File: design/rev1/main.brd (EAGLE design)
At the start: 78 x 50 mm, 43 parts, among them J1 ICSP-HEADER1X6-0.1-ICSP-PADS, J2 HEADER-141X14-0.1-PADS, SW1 JS102000SAQN, SW2 JS102000SAQN, SW3 B3U-3000P, U1 PIC18F2XK20, U2 LIS3DSH, U3 APDS-9008

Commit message: [CNG] - more schematic and layout progress on rev1
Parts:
- added C7: 0.1uF, matt:SMD-0603
- C2: device matt:SMD-0805 -> matt:SMD-0603
- D1, D10, D2, D3, D4, D5, D6, D7, D8, D9: value LED0402 -> LED0603; device matt:SMD-0402-P -> matt:SMD-0603-P
- J2: value HEADER-141X14-0.1-PADS -> HEADER-141X14-0.05-PADS; device matt:1X14-0.1-PADS -> matt:1X14-0.05-PADS
- moved SW3 59.3 mm to (13.0, 48.0), turned to 0 degrees
- moved L1 30.1 mm to (53.7, 26.0)
- moved REG1 30.1 mm to (49.8, 26.6)
- moved R2 30.0 mm to (47.2, 26.6)
- moved R1 30.0 mm to (46.0, 26.6)
- moved C1 30.0 mm to (49.9, 24.2)
- moved C2 30.0 mm to (46.9, 24.2)
- moved U1 15.1 mm to (21.5, 38.0)
- moved C3 11.1 mm to (2.25, 38.0)
- moved R15 9.35 mm to (7.05, 38.0)
- moved C5 8.45 mm to (3.95, 38.0)
- moved U2 7.67 mm to (10.6, 38.0), turned to 90 degrees
- moved R13 7.64 mm to (8.25, 38.0)
- moved C4 6.47 mm to (5.65, 38.0)
- moved SW2 5.50 mm to (52.5, 2.90)
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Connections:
- removed net N$1: B1.P$+, B2.P$+, SW1.SW$3
- new net V_BATT: B1.P$+, B2.P$+, C1.1, L1.P$1, REG1.8, SW1.SW$3
- net +3V3: now also J1.P$2
- net ACCEL_INT1: now also J2.P$4; no longer J2.P$11
- net ACCEL_INT2: now also J2.P$5; no longer J2.P$12
- net GND: now also C7.2, J2.P$1, SW1.SW$1; no longer J2.P$14
- net LIGHT_VSENSE: now also J2.P$6; no longer J2.P$10
- net PIC_CS: now also J2.P$13; no longer J2.P$4
- net PIC_EXT_FUNC: now also J2.P$9; no longer J2.P$13
- net PIC_RX: now also J2.P$3; no longer J2.P$2
- net PIC_SCK: now also J2.P$10; no longer J2.P$5
- net PIC_SDI: now also J2.P$12; no longer J2.P$7
- net PIC_SDO: now also J2.P$11; no longer J2.P$6
- net PIC_TX: now also J2.P$2; no longer J2.P$3
- net PROG_EN: now also J2.P$7; no longer J2.P$9
- net V_SW: now also C7.1, J2.P$14; no longer C1.1, J1.P$2, J2.P$1, L1.P$1, REG1.8
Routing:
- net GND: track 14.2 -> 342.9 mm, vias 0 -> 10
- net +3V3: track 18.1 -> 178.9 mm, vias 2 -> 7
- net V_BATT: track 0.00 -> 88.6 mm, vias 0 -> 3
- net PROG_EN: track 0.00 -> 87.8 mm, vias 0 -> 3
- net V_SW: track 21.7 -> 103.0 mm, vias 2 -> 3
- net PIC_CS: track 0.00 -> 62.1 mm, vias 0 -> 2
- net PIC_SDO: track 0.00 -> 60.2 mm, vias 0 -> 2
- net PIC_SDI: track 0.00 -> 60.1 mm, vias 0 -> 2
- net PIC_SCK: track 0.00 -> 53.9 mm, vias 0 -> 3
- net ACCEL_INT1: track 0.00 -> 48.1 mm, vias 0 -> 5
- net ACCEL_INT2: track 0.00 -> 46.9 mm, vias 0 -> 4
- net ICSP_CLK: track 0.00 -> 46.8 mm, vias 0 -> 2
- net PIC_TX: track 0.00 -> 46.5 mm, vias 0 -> 2
- net ICSP_DAT: track 0.00 -> 45.2 mm, vias 0 -> 2
- net ICSP_!MCLR!: track 0.00 -> 42.8 mm, vias 0 -> 3
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- added copper zone on layer 1, net +3V3
- added copper zone on layer 1, net GND
- added copper zone on layer 1, net N$3
- added copper zone on layer 1, net N$5
- added copper zone on layer 1, net V_BATT
- added copper zone on layer 16, net V_BATT
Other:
- outline, holes or cut-outs redrawn

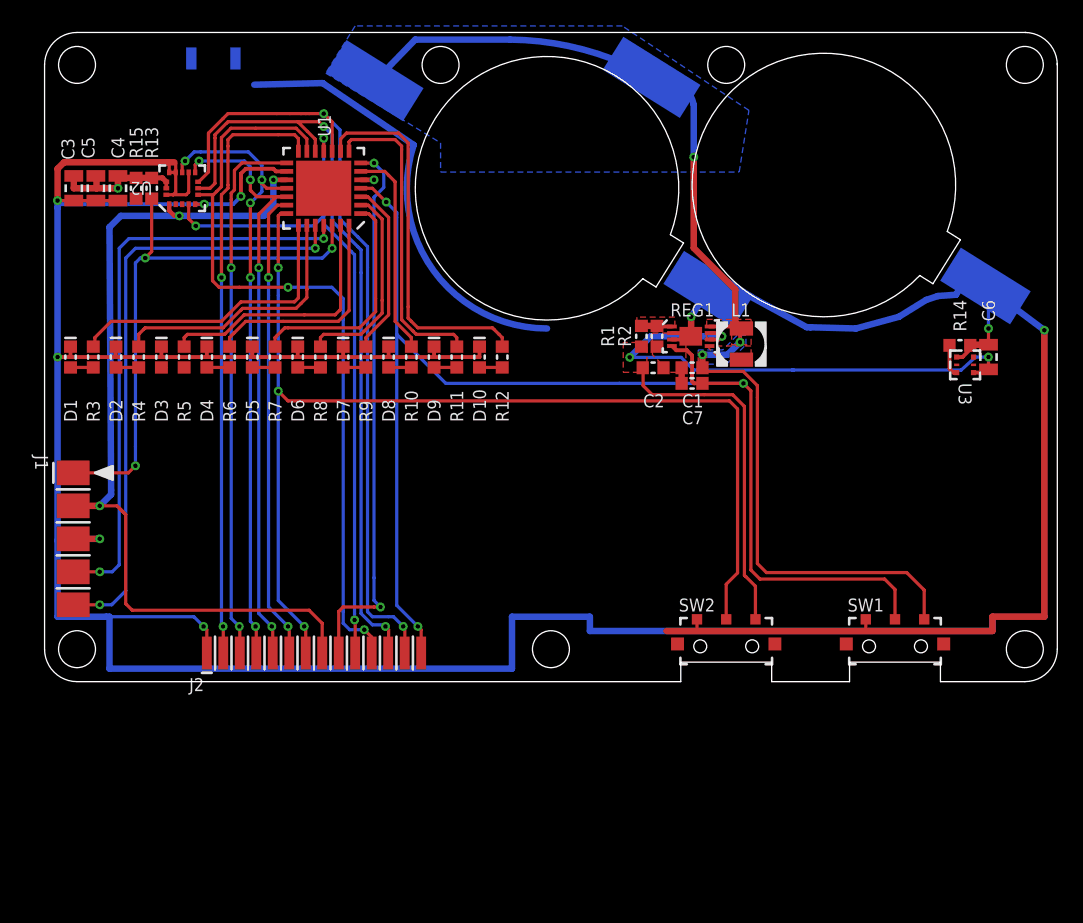
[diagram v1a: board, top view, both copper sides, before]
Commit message: [CNG] - finished most of the new electrical changes for rev1 (see planning.txt), starting layout
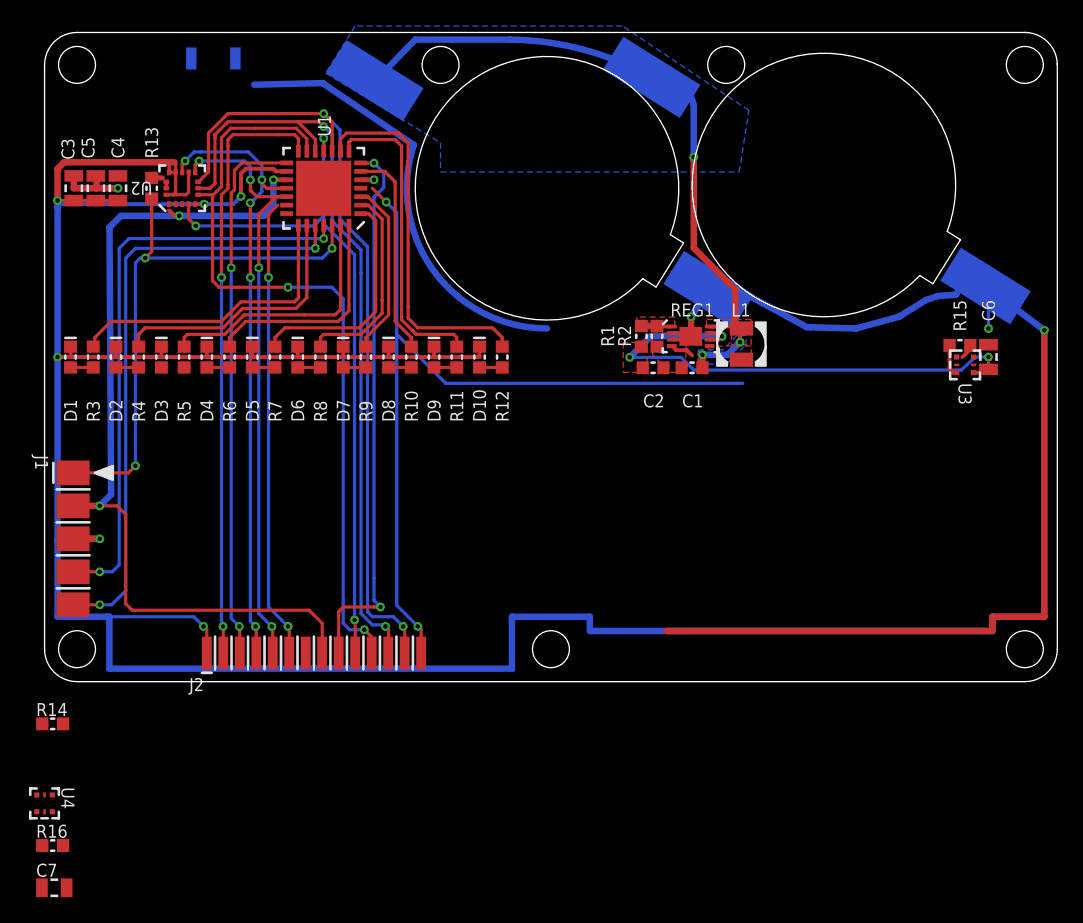
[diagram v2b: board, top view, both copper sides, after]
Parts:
- removed SW2: JS102000SAQN, matt:JS102000SAQN
- removed SW3: B3U-3000P, matt:B3U-3000P
- added R16: 10K, matt:SMD-0603
- added U4: APDS-9008, matt:AVAGO-CHIPLED6
- C7: device matt:SMD-0603 -> matt:SMD-0805
- SW1: value JS102000SAQN -> B3U-3000P; device matt:JS102000SAQN -> matt:B3U-3000P
- moved R14 75.7 mm to (0.62, -3.25), turned to 0 degrees
- moved SW1 69.2 mm to (13.0, 48.0), flipped to the bottom
- moved R15 64.6 mm to (70.5, 25.9), turned to 180 degrees
- moved C7 62.6 mm to (0.75, -15.9), turned to 0 degrees
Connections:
- removed net LIGHT_VSENSE: J2.P$6, R14.2, U1.P$20, U3.P$6
- removed net PROG_EN: J2.P$7, SW2.SW$2, U1.P$21
- removed net V_SW: C7.1, J2.P$14, REG1.4, SW1.SW$2, U1.P$4
- new net ALS_VSENSE_CLK: J2.P$7, R15.2, U1.P$21, U3.P$6
- new net ALS_VSENSE_DAT: J2.P$6, R16.2, U1.P$4, U4.P$6
- new net BOOST_EN: C6.2, C7.2, J2.P$14, R14.2, REG1.4, U1.P$7, U3.P$1, U4.P$1
- net +3V3: no longer C6.2, R15.2, SW2.SW$3, U3.P$1
- net GND: now also C7.1, R15.1, R16.1, U4.P$4; no longer C7.2, SW2.SW$1, SW3.SW$1
- net PIC_EXT_FUNC: now also SW1.SW$2, U1.P$20; no longer R15.1, SW3.SW$2, U1.P$7
- net V_BATT: no longer SW1.SW$3
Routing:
- net V_SW: track 103.0 -> 0.00 mm, vias 3 -> 0
- net PROG_EN: track 87.8 -> 0.00 mm, vias 3 -> 0
- net BOOST_EN: track 0.00 -> 68.7 mm, vias 0 -> 2
- net LIGHT_VSENSE: track 38.6 -> 0.00 mm, vias 2 -> 0
- net ALS_VSENSE_DAT: track 0.00 -> 35.5 mm, vias 0 -> 2
- net V_BATT: track 88.6 -> 54.4 mm
- net +3V3: track 178.9 -> 145.6 mm
- net GND: track 342.9 -> 337.0 mm
- net ALS_VSENSE_CLK: track 0.00 -> 2.47 mm
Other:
- outline, holes or cut-outs redrawn
